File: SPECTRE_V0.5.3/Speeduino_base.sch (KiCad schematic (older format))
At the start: 218 parts, among them J1 Conn_01x06_Male, J2 Conn_02x04_Odd_Even, J3 ProtoArea, Q1 AO3400, Q10 BSP78, Q11 BSP78, Q12 AO3400, Q13 BSP78, Q14 BSP78, Q15 BSP78, Q16 BSP78, Q17 BSP78, Q18 BSP78, Q19 BSP78, Q20 BSP78, Q21 BSP78, Q6 AO3400, Q7 AO3400, U1 MAX9926UAEE+, U10 MIC4427, U2 LM78M05_TO220, U3 TL431DBZ, U4 molex_48pin, U5 TJA1050, U6 MAX3232, U7 MIC4427, U8 MIC4427, U9 MIC4427

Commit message: Done re-routing
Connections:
- net PC7: no longer R83.1
- net PD3: now also R83.1
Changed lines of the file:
@@
 PWR_GND
 Text GLabel 15700 2950 0    50   Input ~ 0
-PC7
+PD3
 Wire Wire Line
 	16300 3300 16150 3300

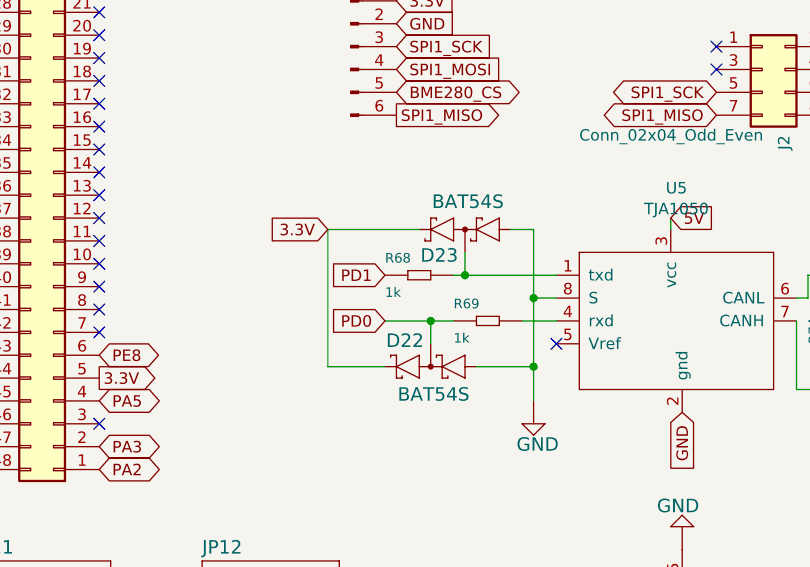
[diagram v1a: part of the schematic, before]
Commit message: Update Canbus interface
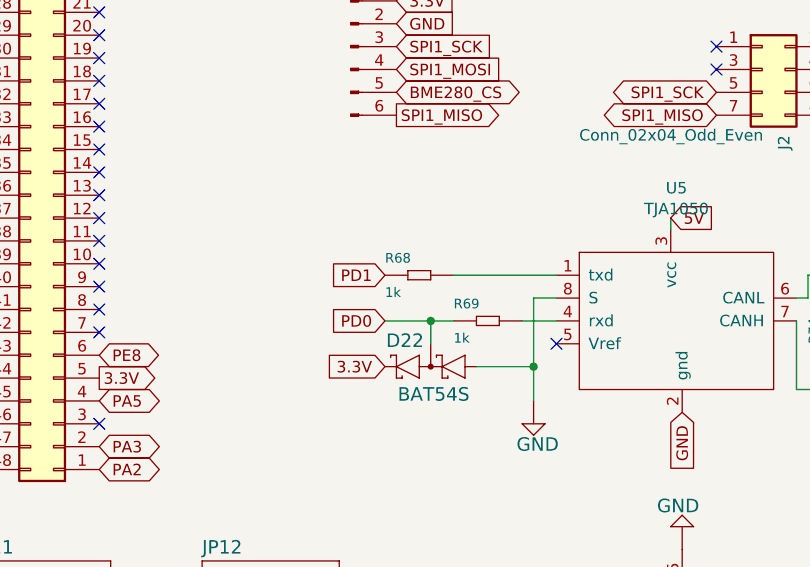
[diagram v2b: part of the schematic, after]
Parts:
- removed D23: BAT54S, Speeduino_base:SOT23, symbol Speeduino_base-eagle-import:BAT54S
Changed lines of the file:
@@
 $EndComp
 $Comp
-L Speeduino_base-eagle-import:SMD-RES-470R-5%-1_10W(0603) R68
-U 1 1 5E97D64D
-P 12600 7650
-F 0 "R68" H 12450 7700 42  0000 L BNN
-F 1 "1k" H 12450 7550 42  0000 L BNN
-F 2 "Speeduino_base:R0603" H 12600 7650 50  0001 C CNN
-F 3 "" H 12600 7650 50  0001 C CNN
-	1    12600 7650
-	1    0    0    -1
-$EndComp
-$Comp
 L Speeduino_base-eagle-import:BAT54S D19
 U 1 1 20478EC3
@@
 $EndComp
 $Comp
-L Speeduino_base-eagle-import:BAT54S D23
-U 1 1 5E8B9631
-P 12800 7450
-F 0 "D23" H 12830 7529 59  0000 L BNN
-F 1 "BAT54S" H 12630 7294 59  0000 L BNN
-F 2 "Speeduino_base:SOT23" H 12800 7450 50  0001 C CNN
-F 3 "" H 12800 7450 50  0001 C CNN
-	1    12800 7450
-	-1   0    0    1
-$EndComp
-$Comp
 L Interface_UART:MAX3232 U6
 U 1 1 5E8991D1
@@
 	12750 7850 12650 7850
 Wire Wire Line
-	12800 7550 12800 7650
-Wire Wire Line
 	12650 7950 12650 7850
 Connection ~ 12650 7850
@@
 	12650 7850 12450 7850
 Wire Wire Line
-	12750 7650 12800 7650
-Connection ~ 12800 7650
-Wire Wire Line
-	12800 7650 13200 7650
-Wire Wire Line
-	13000 7450 13100 7450
-Wire Wire Line
-	13100 7450 13100 7750
-Wire Wire Line
 	12850 8050 13100 8050
 Connection ~ 13100 8050
@@
 Wire Wire Line
 	13200 7750 13100 7750
-Connection ~ 13100 7750
 Wire Wire Line
 	13100 7750 13100 8050
-Wire Wire Line
-	12450 8050 12200 8050
-Wire Wire Line
-	12200 8050 12200 7450
-Wire Wire Line
-	12200 7450 12600 7450
-Text GLabel 12200 7450 0    50   Input ~ 0
+Text GLabel 12450 8050 0    50   Input ~ 0
 3.3V
 Wire Wire Line
@@
 	0    -1   -1   0
 $EndComp
+$Comp
+L Speeduino_base-eagle-import:SMD-RES-470R-5%-1_10W(0603) R68
+U 1 1 5E97D64D
+P 12600 7650
+F 0 "R68" H 12450 7700 42  0000 L BNN
+F 1 "1k" H 12450 7550 42  0000 L BNN
+F 2 "Speeduino_base:R0603" H 12600 7650 50  0001 C CNN
+F 3 "" H 12600 7650 50  0001 C CNN
+	1    12600 7650
+	1    0    0    -1
+$EndComp
+Wire Wire Line
+	12750 7650 13200 7650
 $EndSCHEMATC
